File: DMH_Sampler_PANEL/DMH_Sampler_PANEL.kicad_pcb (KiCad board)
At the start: 2 copper layers, 50 x 200 mm, 5 parts, among them J0 Panel_GND_Solder_Wire_Pad

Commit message: Panel experiments in progress
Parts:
- added H10: Speed, SynthStuff:Jack_6.35mm_Cutout_v3, F.Cu at (186.5, 126.8)
- added H11: Size / End Pos, SynthStuff:Pot_Cutout_Small, F.Cu at (128.0, 101.0)
- added H12: Start Pos, SynthStuff:Pot_Cutout_Small, F.Cu at (128.0, 130.5)
- added H13: Speed, SynthStuff:Pot_Cutout_Small, F.Cu at (128.0, 160.0)
- added H14: Trig Mode, SynthStuff:Toggle_Switch_TE_Cutout, F.Cu at (151.2, 93.7)
- added H15: Pb Mode, SynthStuff:Toggle_Switch_TE_Cutout, F.Cu at (166.3, 93.7)
- added H16: Rec Mode, SynthStuff:Toggle_Switch_TE_Cutout, F.Cu at (181.3, 93.7)
- added H17: CV Amt, SynthStuff:Toggle_Switch_TE_Cutout, F.Cu at (196.3, 93.7)
- added H18: Size Mode, SynthStuff:Toggle_Switch_TE_Cutout, F.Cu at (211.3, 93.7)
- added H19: Play, SynthStuff:MX_switch_Cutout, F.Cu at (153.8, 145.4)
- added H20: Rec, SynthStuff:MX_switch_Cutout, F.Cu at (153.8, 165.5)
- added H5: Audio In, SynthStuff:Jack_6.35mm_Cutout_v3, F.Cu at (152.3, 109.7)
- added H6: Audio Out, SynthStuff:Jack_6.35mm_Cutout_Output_v6, F.Cu at (152.3, 126.8)
- added H7: Trigger, SynthStuff:Jack_6.35mm_Cutout_v3, F.Cu at (169.4, 109.7)
- added H8: Start, SynthStuff:Jack_6.35mm_Cutout_v3, F.Cu at (169.4, 126.8)
- added H9: End, SynthStuff:Jack_6.35mm_Cutout_v3, F.Cu at (186.5, 109.7)
- added J1: USB_C_Receptacle_USB2.0_16P, Connector_USB:USB_C_Receptacle_G-Switch_GT-USB-7051x, F.Cu at (133.2, 193.5)
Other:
- board text added: "24F"
- board text added: "Sampler"
- board text removed: "Module Name"
- board text removed: "TYPE"

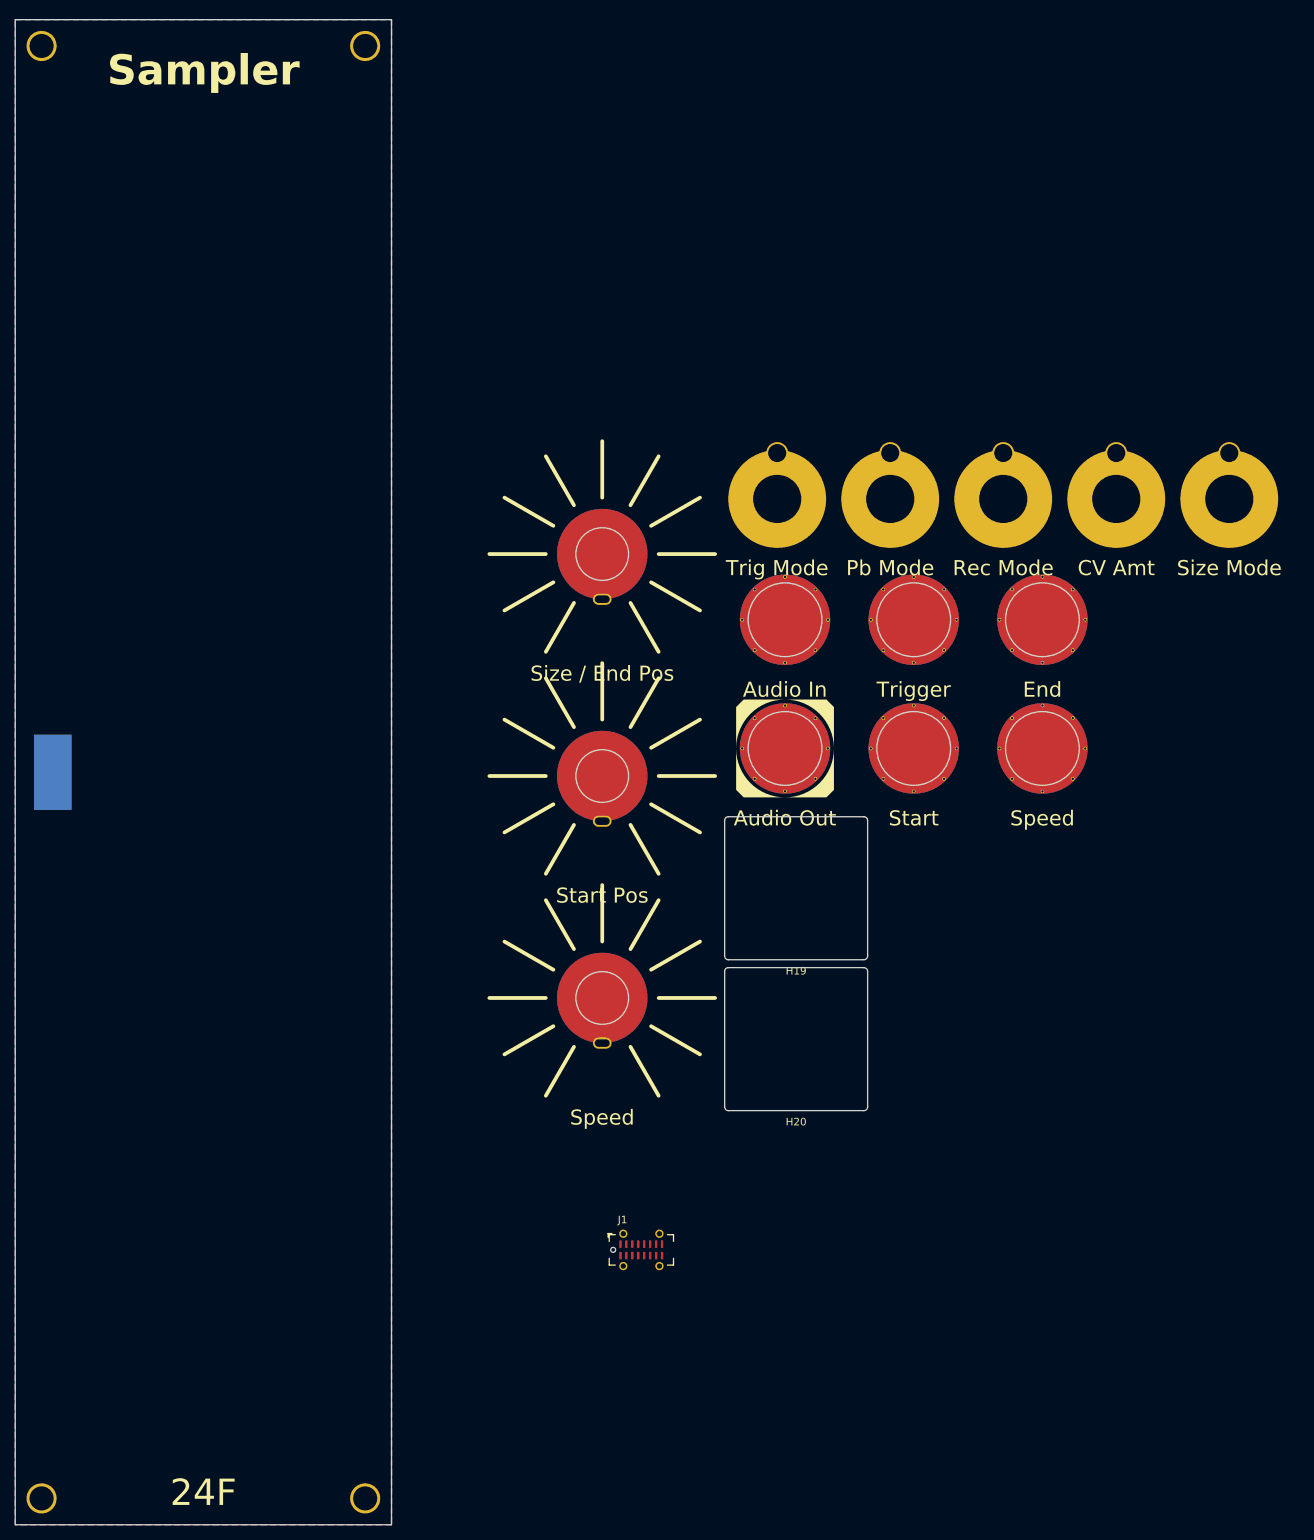
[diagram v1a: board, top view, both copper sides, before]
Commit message: Designed front panel
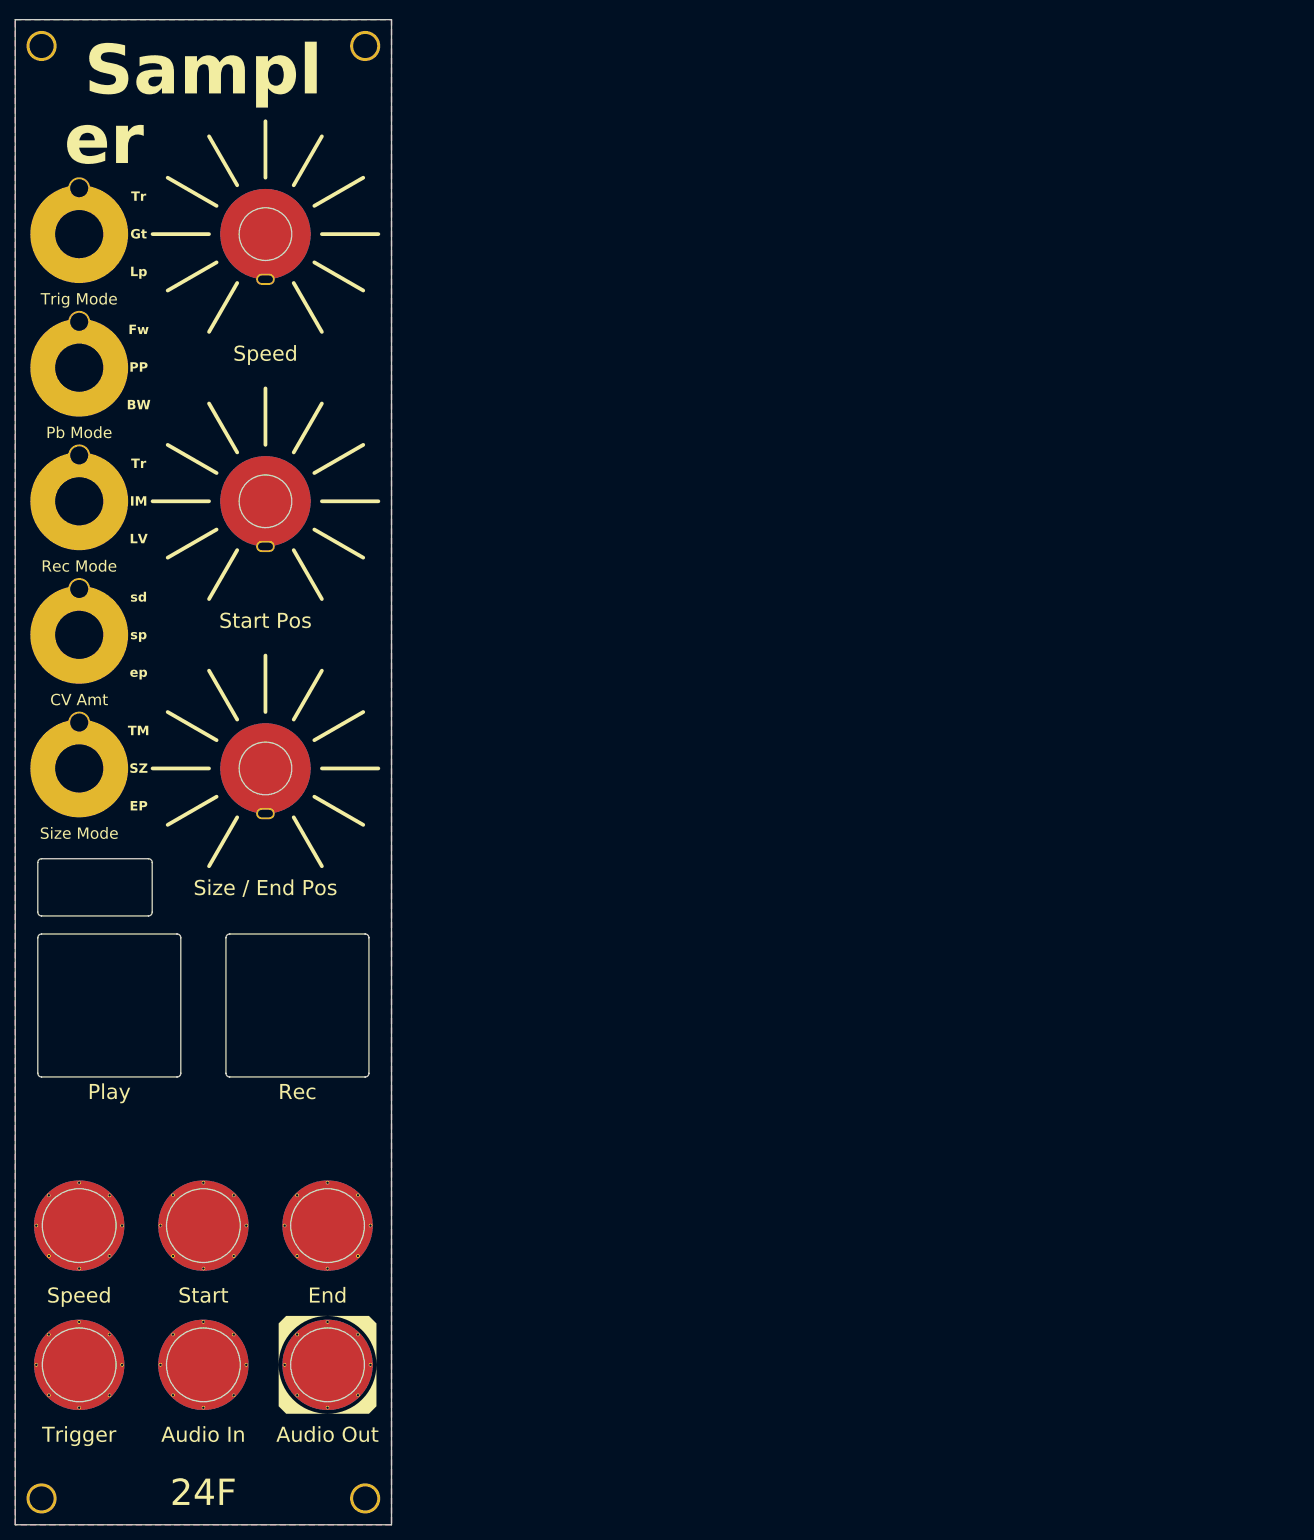
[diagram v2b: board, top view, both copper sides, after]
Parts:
- removed J0: Panel_GND_Solder_Wire_Pad, SynthStuff:Panel_GND_SolderWirePad_5x10mm
- removed J1: USB_C_Receptacle_USB2.0_16P, Connector_USB:USB_C_Receptacle_G-Switch_GT-USB-7051x
- added H21: USB_A, SynthStuff:USB-A_Cutout, F.Cu at (60.6, 145.3)
- moved H18 157.0 mm to (58.5, 129.5)
- moved H7 148.7 mm to (58.5, 208.8)
- moved H10 142.8 mm to (58.5, 190.2)
- moved H17 139.0 mm to (58.5, 111.8)
- moved H5 125.6 mm to (75.0, 208.8)
- moved H9 124.5 mm to (91.5, 190.2)
- moved H16 122.8 mm to (58.5, 94.0)
- moved H8 113.7 mm to (75.0, 190.2)
- moved H13 110.9 mm to (83.2, 58.5)
- moved H15 109.2 mm to (58.5, 76.2)
- moved H6 102.0 mm to (91.5, 208.8)
- moved H14 99.2 mm to (58.5, 58.5)
- moved H19 92.6 mm to (62.5, 161.0)
- moved H20 66.4 mm to (87.5, 161.0)
- moved H12 57.8 mm to (83.2, 94.0)
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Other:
- board text added: "BW"
- board text added: "EP"
- board text added: "Fw"
- board text added: "Gt"
- board text added: "IM"
- board text added: "LV"
- board text added: "Lp"
- board text added: "PP"
- board text added: "SZ"
- board text added: "Sampl"
- board text added: "TM"
- board text added: "Tr"
- board text added: "ep"
- board text added: "er"
- board text added: "sd"
- board text added: "sp"
- board text removed: "Sampler"

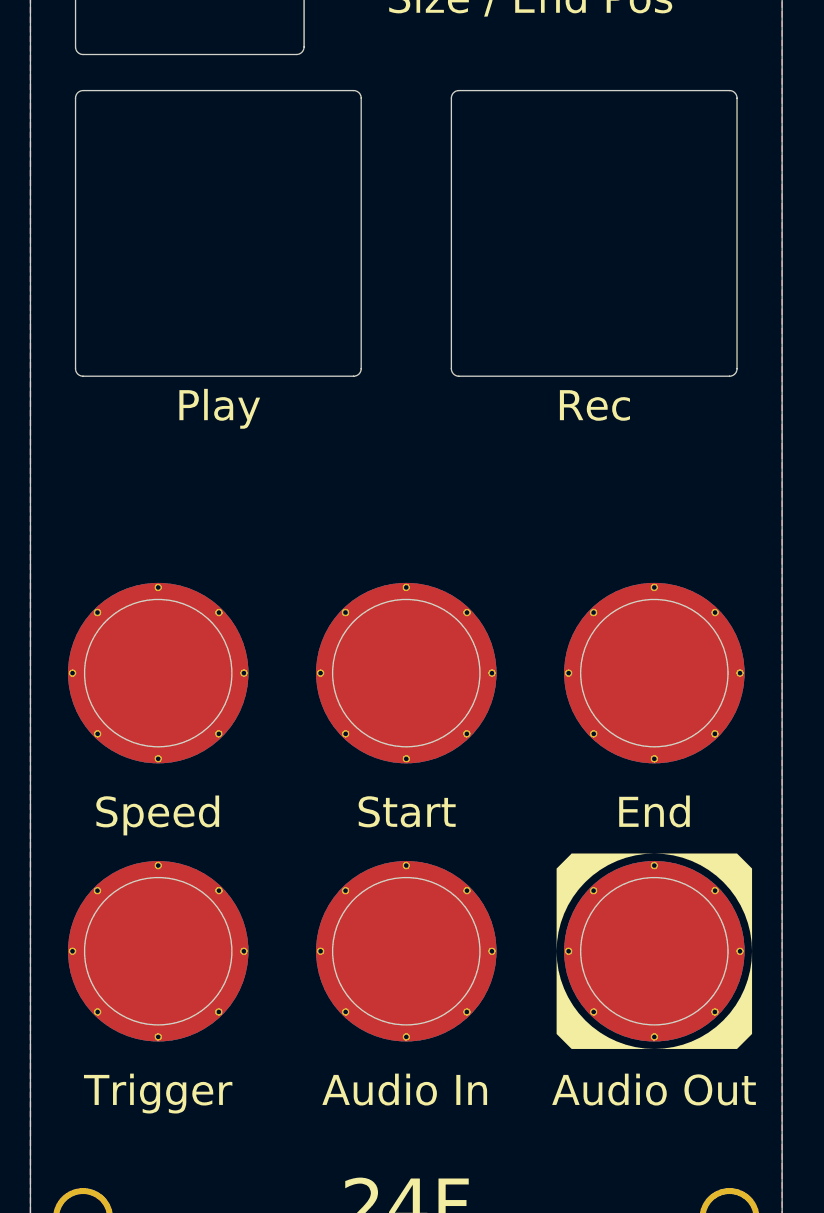
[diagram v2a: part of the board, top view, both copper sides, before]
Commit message: Added solder mask cutouts for LEDs
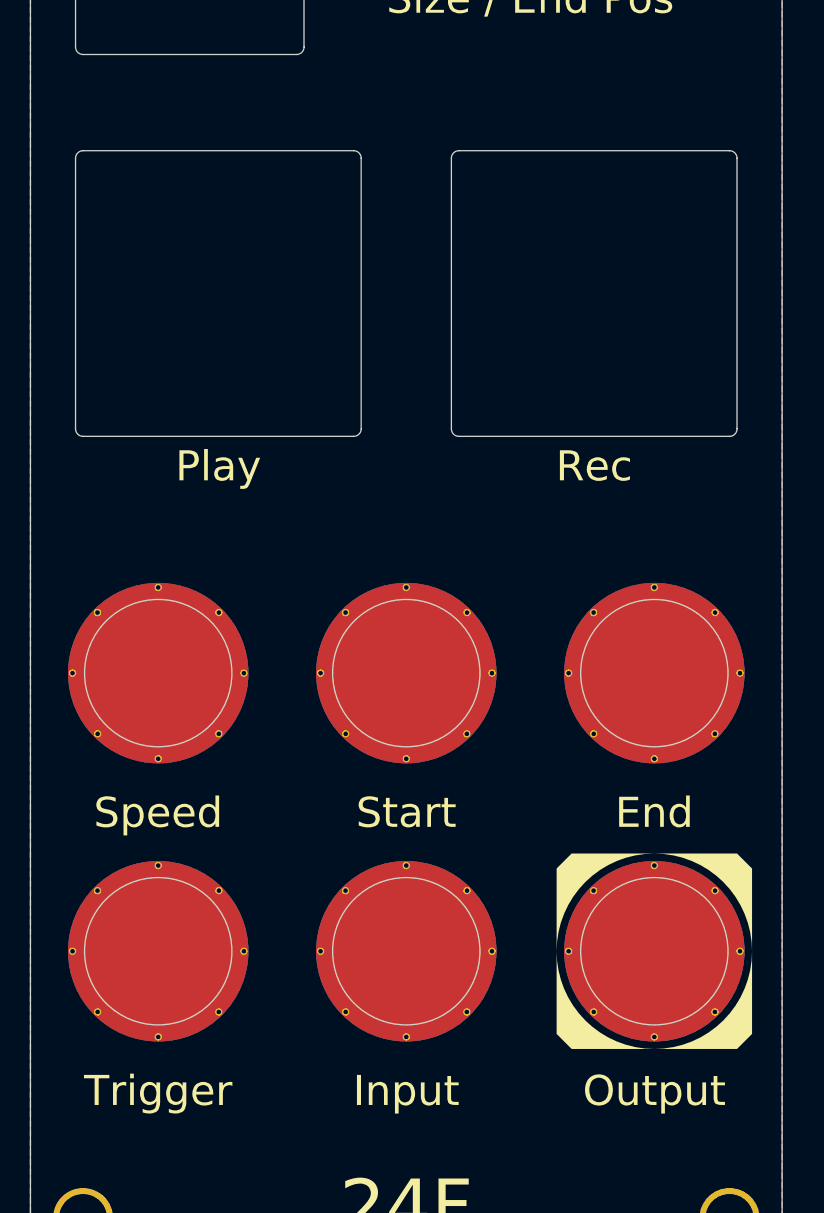
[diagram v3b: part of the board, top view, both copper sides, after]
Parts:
- H5: value Audio In -> Input
- H6: value Audio Out -> Output
- moved H19 4.00 mm to (62.5, 165.0)
- moved H20 4.00 mm to (87.5, 165.0)
